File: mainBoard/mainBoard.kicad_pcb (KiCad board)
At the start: 4 copper layers, 128.2 x 64.5 mm, 76 parts, among them J1 Conn_01x01, J10 Conn_01x05, J11 Conn_01x04, J12 Conn_01x01, J13 Conn_01x01, J14 Conn_01x01, J15 Conn_01x01, J16 Conn_01x01, J17 Conn_01x01, J18 Conn_01x01, J19 Conn_01x01, J2 Conn_01x01, J20 Conn_01x01, J21 Conn_01x01, J22 Conn_01x01, J23 Conn_01x05, J24 Conn_01x04, J25 Conn_01x05, J26 Conn_01x05, J27 Conn_01x05, J28 Conn_01x04, J29 Conn_01x04, J3 Conn_01x01, J30 Conn_01x04, J31 Conn_02x05_Odd_Even, J32 Conn_02x07_Odd_Even, J33 Conn_01x04, J34 Conn_01x02, J35 Conn_01x02, J36 Conn_01x03, J37 Conn_01x02, J38 Conn_01x02, J4 Conn_01x01, J5 Conn_01x01, J6 Conn_01x01, J7 Conn_01x01, J8 Conn_01x01, J9 Conn_01x01, M1 Conn_01x01, M2 Conn_01x01, U1 STM32H503CBT6, U2 DRV8251ADDAR, U3 MAX15062A, U4 64Kbit

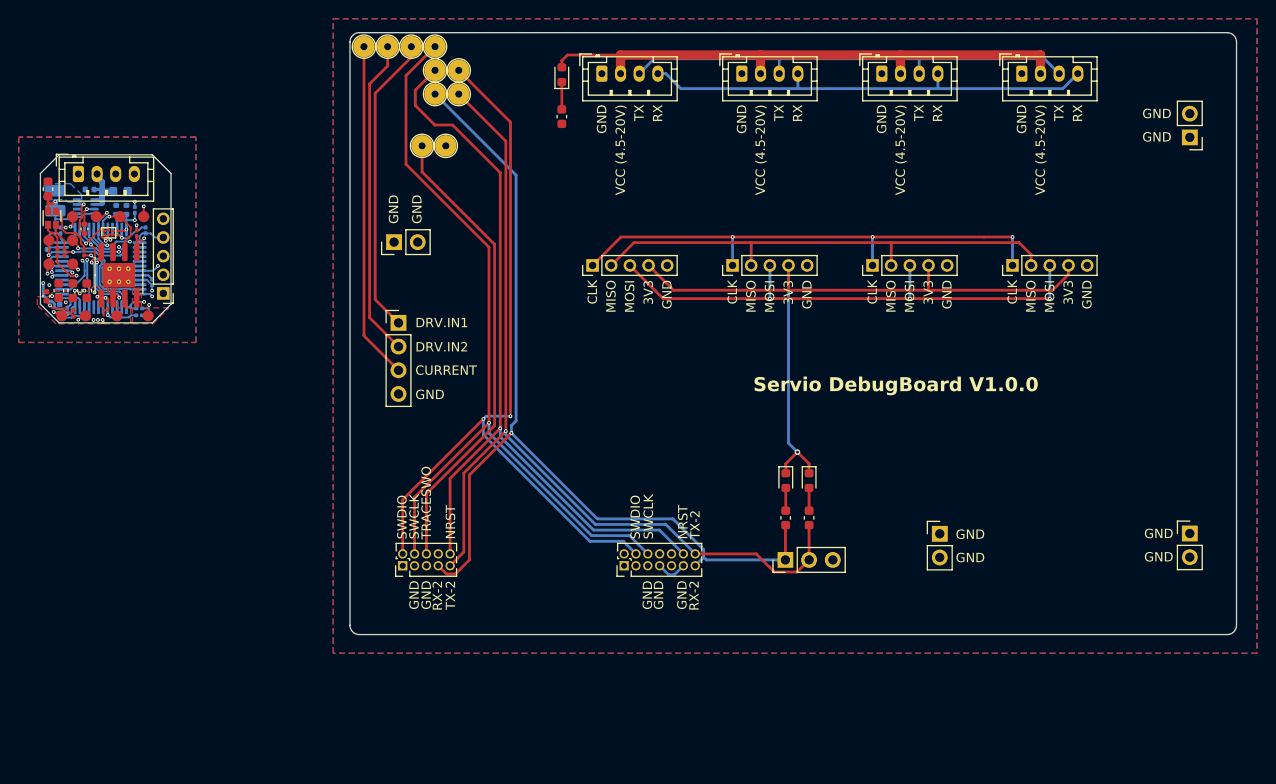
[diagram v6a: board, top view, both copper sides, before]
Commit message: Reducing size of debug board
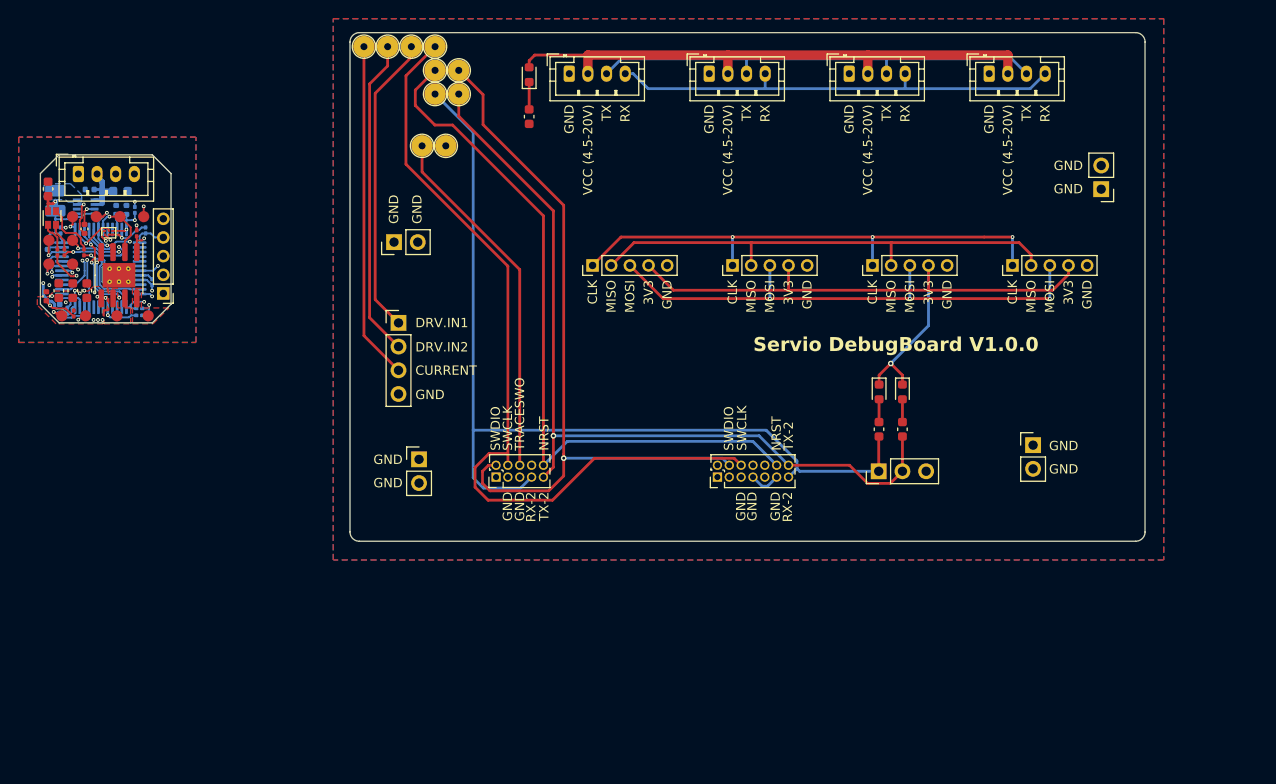
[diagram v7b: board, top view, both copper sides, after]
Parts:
- moved J34 83.0 mm to (134.2, 97.2)
- moved D3 13.8 mm to (186.0, 90.0)
- moved D4 13.8 mm to (183.5, 90.0)
- moved J31 13.8 mm to (142.4, 99.1)
- moved J32 13.8 mm to (166.2, 99.1)
- moved J36 13.8 mm to (183.5, 98.5)
- moved J37 13.8 mm to (200.0, 95.7)
- moved R8 13.8 mm to (183.5, 94.0)
- moved R9 13.8 mm to (186.0, 94.0)
- moved J35 11.0 mm to (207.3, 68.3)
- moved D2 3.50 mm to (146.0, 56.0)
- moved J24 3.50 mm to (150.3, 55.9)
- moved J28 3.50 mm to (165.3, 55.9)
- moved J29 3.50 mm to (195.3, 55.9)
- moved J30 3.50 mm to (180.3, 55.9)
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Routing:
- net /DebuBoard/DB-TUNING-LINES.TRACESWO: track 50.0 -> 38.6 mm
- net /DebuBoard/DB-TUNING-LINES.TX-2: track 98.4 -> 89.5 mm
- net /DebuBoard/DB-TUNING-LINES.NRST: track 85.5 -> 77.1 mm, vias 1 -> 0
- net /DebuBoard/3V3: track 79.1 -> 70.9 mm
- net /DebuBoard/DB-TUNING-LINES.SWDIO: track 83.7 -> 78.9 mm, vias 2 -> 1
- net /DebuBoard/DB-TUNING-LINES.SWCLK: track 86.1 -> 88.2 mm, vias 1 -> 0
- net /DebuBoard/DB-TUNING-LINES.RX-2: track 100.5 -> 100.8 mm, vias 1 -> 0
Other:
- board size 128.2 x 64.5 mm -> 118.4 x 54.5 mm

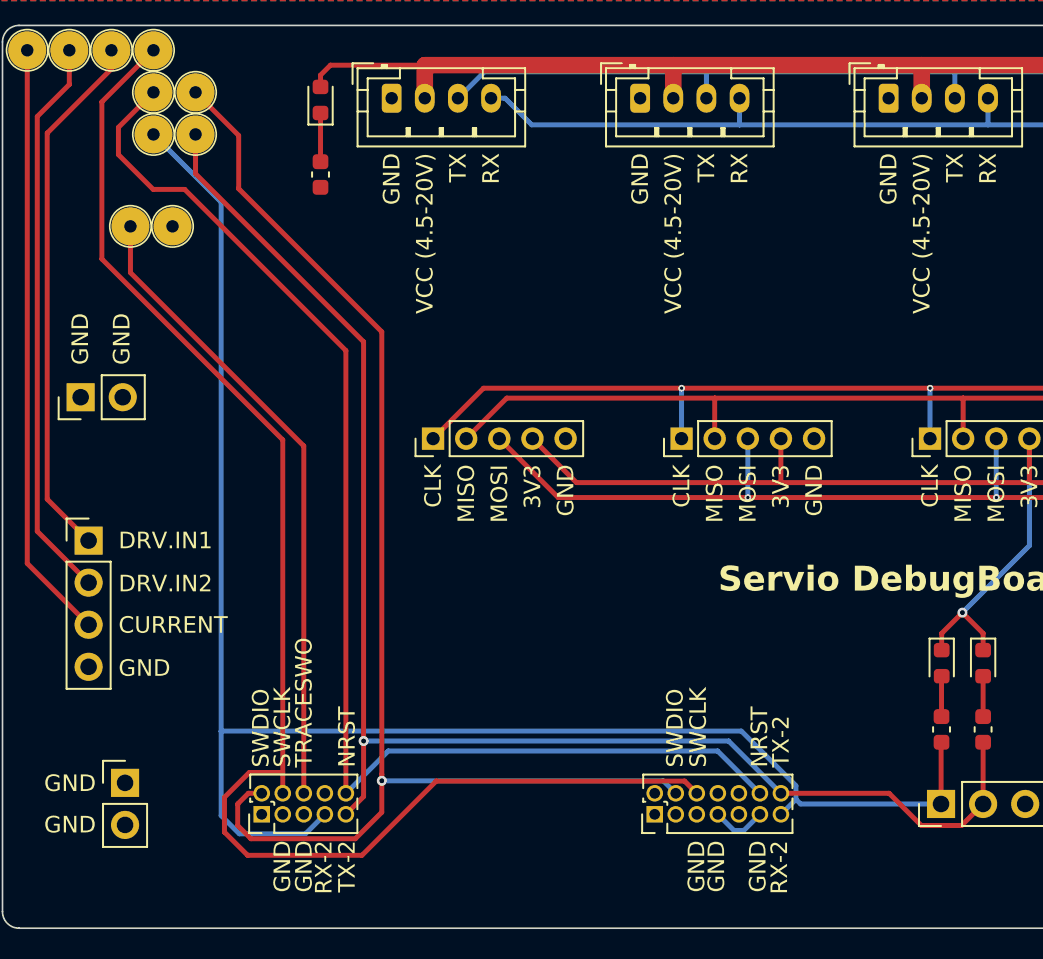
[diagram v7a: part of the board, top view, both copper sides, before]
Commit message: Fix GND polygon
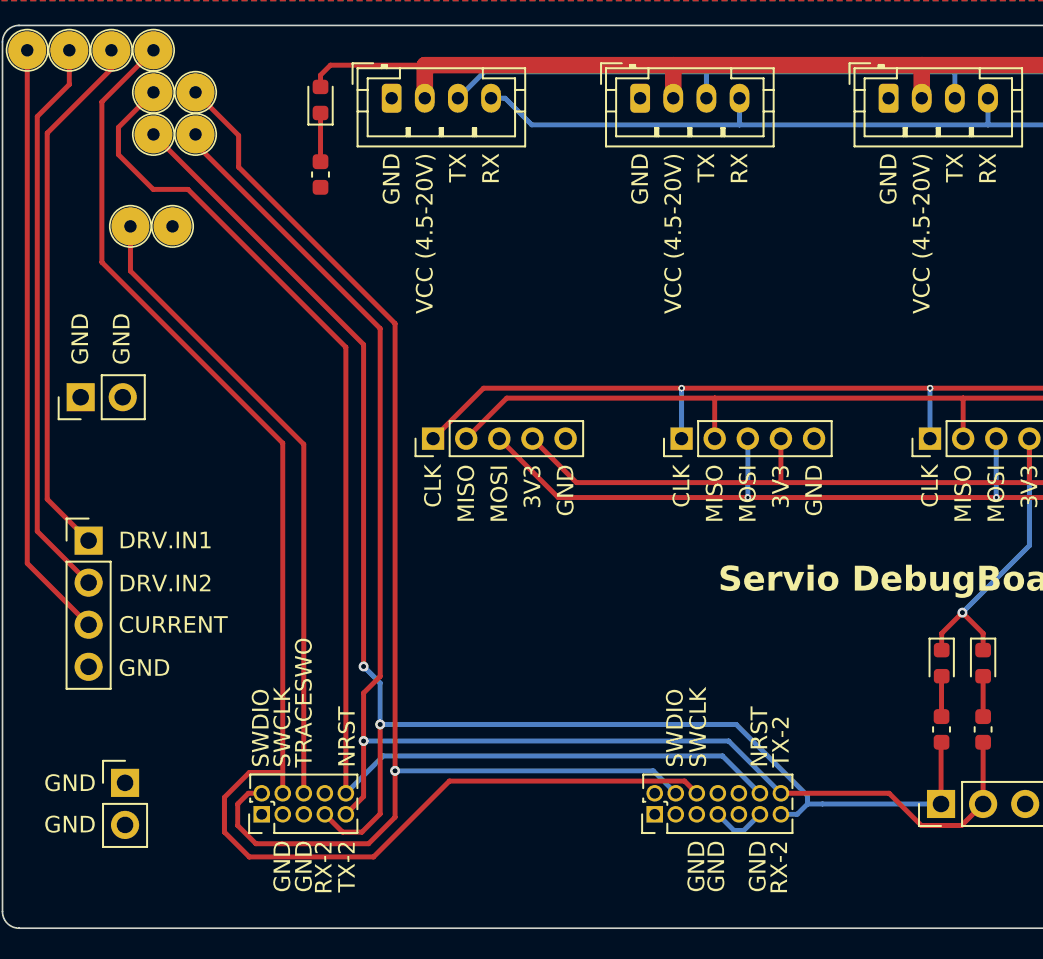
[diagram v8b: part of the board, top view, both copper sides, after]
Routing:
- net /DebuBoard/DB-TUNING-LINES.RX-2: track 100.8 -> 92.7 mm, vias 0 -> 2
- net /DebuBoard/DB-TUNING-LINES.SWDIO: track 78.9 -> 79.9 mm
- net /DebuBoard/DB-TUNING-LINES.TX-2: track 89.5 -> 90.3 mm
